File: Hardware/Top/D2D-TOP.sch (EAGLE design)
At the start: 54 parts, among them SW1 SWITCH.MOM, SW2 SWITCH.MOM, U2 NRF52832_MODULE_MDBT42, U4 PCF8523, U6 PHOTOTRANSISTOR

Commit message: current top and bottom board
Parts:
- added SW5: SWITCH.MOM, LinnesLab-Switches:SWITCH.MOM
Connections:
- removed net VBATT: U4.VBAT
- net GND: now also SW5.3, SW5.4, USB2.SHIELD
- net SW1: now also SW5.1
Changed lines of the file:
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@@
 <part name="SW2" library="LinnesLab-Switches" deviceset="SWITCH.MOM" device=""/>
 <part name="GND2" library="LinnesLab-Symbols" deviceset="GND" device=""/>
+<part name="SW5" library="LinnesLab-Switches" deviceset="SWITCH.MOM" device=""/>
+<part name="GND5" library="LinnesLab-Symbols" deviceset="GND" device=""/>
 </parts>
 <sheets>
@@
 <attribute name="VALUE" x="320.04" y="25.146" size="1.778" layer="96" align="top-center"/>
 </instance>
+<instance part="SW5" gate="G$1" x="347.98" y="33.02" smashed="yes">
+<attribute name="NAME" x="347.98" y="37.846" size="1.778" layer="95" font="vector" align="bottom-center"/>
+<attribute name="VALUE" x="347.98" y="30.226" size="1.778" layer="96" font="vector" align="top-center"/>
+</instance>
+<instance part="GND5" gate="G$1" x="355.6" y="25.4" smashed="yes">
+<attribute name="VALUE" x="355.6" y="25.146" size="1.778" layer="96" align="top-center"/>
+</instance>
 </instances>
 <busses>
@@
 <pinref part="GND40" gate="G$1" pin="GND"/>
 <wire x1="40.64" y1="-68.58" x2="40.64" y2="-76.2" width="0.1524" layer="91"/>
+<pinref part="USB2" gate="G$1" pin="SHIELD"/>
+<wire x1="38.1" y1="-55.88" x2="40.64" y2="-55.88" width="0.1524" layer="91"/>
+<wire x1="40.64" y1="-55.88" x2="40.64" y2="-68.58" width="0.1524" layer="91"/>
+<junction x="40.64" y="-68.58"/>
 </segment>
 <segment>
@@
 <wire x1="317.5" y1="30.48" x2="320.04" y2="30.48" width="0.1524" layer="91" style="longdash"/>
 <junction x="320.04" y="30.48"/>
+</segment>
+<segment>
+<pinref part="SW5" gate="G$1" pin="3"/>
+<pinref part="GND5" gate="G$1" pin="GND"/>
+<wire x1="353.06" y1="33.02" x2="355.6" y2="33.02" width="0.1524" layer="91" style="longdash"/>
+<wire x1="355.6" y1="33.02" x2="355.6" y2="30.48" width="0.1524" layer="91" style="longdash"/>
+<pinref part="SW5" gate="G$1" pin="4"/>
+<wire x1="355.6" y1="30.48" x2="355.6" y2="27.94" width="0.1524" layer="91" style="longdash"/>
+<wire x1="353.06" y1="30.48" x2="355.6" y2="30.48" width="0.1524" layer="91" style="longdash"/>
+<junction x="355.6" y="30.48"/>
 </segment>
 </net>
@@
 </segment>
 </net>
-<net name="VBATT" class="0">
-<segment>
-<wire x1="284.48" y1="-17.78" x2="281.94" y2="-17.78" width="0.1524" layer="91"/>
-<label x="281.94" y="-17.78" size="1.27" layer="95" rot="R180" xref="yes"/>
-<pinref part="U4" gate="G$1" pin="VBAT"/>
-</segment>
-</net>
 <net name="OUTPUT" class="0">
 <segment>
@@
 <label x="304.8" y="33.02" size="1.27" layer="95" ratio="15" rot="R180" xref="yes"/>
 </segment>
-</net>
+<segment>
+<pinref part="SW5" gate="G$1" pin="1"/>
+<wire x1="342.9" y1="33.02" x2="340.36" y2="33.02" width="0.1524" layer="91"/>
+<label x="340.36" y="33.02" size="1.27" layer="95" ratio="15" rot="R180" xref="yes"/>
+</segment>
+</net>

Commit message: unfinished 002
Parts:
- removed SW5: SWITCH.MOM, LinnesLab-Switches:SWITCH.MOM
- added C23: 100n, LinnesLab-Passives:CAPACITOR0603
- added C24, C25: 47p, LinnesLab-Passives:CAPACITOR0603
- added J1: (no value), LinnesLab-Connectors:CONN_07
- added JP2: (no value), LinnesLab-Switches:JUMPER-SMT_2_NO_SILK
- added LED5: RED, LinnesLab-LED:LED0603
- added LED6: YELLOW, LinnesLab-LED:LED0603
- added R1, R2: 0, LinnesLab-Passives:RESISTOR0603
- added R18, R19: 27, LinnesLab-Passives:RESISTOR0603
- added R20, R21: 1k, LinnesLab-Passives:RESISTOR0603
- added U5: FT231XS, LinnesLab-DigitalIC:FT231XS
- R9: value 10k -> (none)
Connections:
- removed net BATT: R13.1, R14.2
- removed net CHRG.STAT: CHRG2.STAT, R12.1
- removed net RXD: U2.P0.08
- removed net TXD: U2.P0.06
- new net A4/BATT: R13.1, R14.2, U2.P0.28/AIN4
- new net CTS: JP2.2, U5.!CTS
- new net D27/CHRGSTATUS: CHRG2.STAT, R12.1, U2.P0.27
- new net FT3V3: U5.3V3OUT
- new net N$23: R18.2, U5.USBDM
- new net N$24: R19.2, U5.USBDP
- new net N$25: LED5.C, R20.2
- new net N$26: LED6.C, R21.2
- new net RXD.FT: R2.1, U5.RXD
- new net RXD.NRF: R1.2, U2.P0.08
- new net RXLED: R20.1, U5.CBUS1
- new net TXD.FT: R1.1, U5.TXD
- new net TXD.NRF: R2.2, U2.P0.06
- new net TXLED: R21.1, U5.CBUS2
- net 3.3V: now also C23.2, LED5.A, LED6.A, U5.!RESET, U5.VCCIO
- net DTR: now also U5.!DTR
- net GND: now also C23.1, C24.2, C25.1, JP2.1, U5.GND@16, U5.GND@6; no longer SW5.3, SW5.4
- net SCL: now also R9.1; no longer R8.1
- net SDA: now also R8.1; no longer R9.1
- net SW1: no longer SW5.1
- net USB+: now also C24.1, R19.1
- net USB-: now also C25.2, R18.1
- net V_USB: now also U5.VCC
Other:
- note added: "I don't remember if CTS needs to be grounded or left floating so here's a jumper to ground so it can be configued either way dynamically."
- note added: "TXD goes to RX on the other device RXD goes to TX on the other device"
- moved on the sheet: R8, R9

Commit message: updated to 002
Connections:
- removed net CD1: SD2.CARD_DETECT
- removed net CS.OLED: U3./CS
- removed net DC.OLED: U3.DC/I2C_SA0
- removed net RESET.OLED: U3./RES
- removed net SD.CS: SD2.CS
- removed net SW1: SW1.1, SW2.1
- new net A6/TIA: J1.5, U2.P0.30/AIN6
- new net A7/PPG: J1.7, U2.P0.31/AIN7
- new net D11/SW1: SW1.1, U2.P0.11
- new net D15/SW2: SW2.1, U2.P0.15
- new net D16/CS.OLED: U2.P0.16, U3./CS
- new net D29/LED.CTRL: J1.6, U2.P0.29/AIN5
- new net D3/RESET.OLED: U2.P0.03/AIN1, U3./RES
- new net D4/DC.OLED: U2.P0.04/AIN2, U3.DC/I2C_SA0
- new net D5/CD1: SD2.CARD_DETECT, U2.P0.05/AIN3
- new net D7/SD.CS: SD2.CS, U2.P0.07
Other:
- note added: "FTDI Serial to USB Converter"
- moved on the sheet: C23, C24, C25, J1, JP2, LED5, LED6, R1, R18, R19, R2, R20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

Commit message: checkpoint 3
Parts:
- J1: device LinnesLab-Connectors:CONN_07 -> LinnesLab-Connectors:CONN_07-1.27MM
- renumbered CHRG2 to CHRG
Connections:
- net 3.3V: now also J1.4
- net A6/TIA: now also J1.6; no longer J1.5
- net D29/LED.CTRL: now also J1.5; no longer J1.6
- net GND: now also J1.3
- net SCL: now also J1.2
- net SDA: now also J1.1
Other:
- note added: "Connection to top board"
- moved on the sheet: J1
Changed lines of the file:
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@@
 <part name="GND22" library="LinnesLab-Symbols" deviceset="GND" device=""/>
 <part name="SD2" library="LinnesLab-Connectors" deviceset="MICROSD" device="" package3d_urn="urn:adsk.eagle:package:17873109/2"/>
-<part name="CHRG2" library="LinnesLab-Power" deviceset="MCP73831" device=""/>
+<part name="CHRG" library="LinnesLab-Power" deviceset="MCP73831" device=""/>
 <part name="LDO2" library="LinnesLab-Power" deviceset="MIC5504" device=""/>
 <part name="D4" library="LinnesLab-DiscreteSemi" deviceset="SCHOTTKY" device="-USC" package3d_urn="urn:adsk.eagle:package:15664784/2"/>
@@
 <part name="SUPPLY1" library="LinnesLab-Symbols" deviceset="3.3V" device=""/>
 <part name="SUPPLY6" library="LinnesLab-Symbols" deviceset="3.3V" device=""/>
-<part name="J1" library="LinnesLab-Connectors" deviceset="CONN_07" device=""/>
+<part name="J1" library="LinnesLab-Connectors" deviceset="CONN_07" device="-1.27MM"/>
+<part name="SUPPLY8" library="LinnesLab-Symbols" deviceset="3.3V" device=""/>
+<part name="GND5" library="LinnesLab-Symbols" deviceset="GND" device=""/>
 </parts>
 <sheets>
@@
 <wire x1="-40.64" y1="208.28" x2="172.72" y2="208.28" width="1.27" layer="97" style="longdash"/>
 <wire x1="172.72" y1="208.28" x2="172.72" y2="198.12" width="1.27" layer="97" style="longdash"/>
+<text x="7.62" y="223.52" size="1.27" layer="96">Connection to
+top board</text>
 </plain>
 <instances>
@@
 <attribute name="VALUE" x="210.82" y="-3.81" size="1.778" layer="96"/>
 </instance>
-<instance part="CHRG2" gate="G$1" x="96.52" y="-60.96" smashed="yes">
+<instance part="CHRG" gate="G$1" x="96.52" y="-60.96" smashed="yes">
 <attribute name="NAME" x="88.9" y="-55.372" size="1.778" layer="95"/>
 <attribute name="VALUE" x="88.9" y="-68.58" size="1.778" layer="96"/>
@@
 <attribute name="VALUE" x="-12.7" y="172.974" size="1.778" layer="96" align="bottom-center"/>
 </instance>
-<instance part="J1" gate="G$1" x="-10.16" y="241.3" smashed="yes">
-<attribute name="VALUE" x="-15.24" y="231.394" size="1.778" layer="96" font="vector"/>
-<attribute name="NAME" x="-15.24" y="254.508" size="1.778" layer="95" font="vector"/>
+<instance part="J1" gate="G$1" x="12.7" y="241.3" smashed="yes">
+<attribute name="VALUE" x="7.62" y="231.394" size="1.778" layer="96" font="vector"/>
+<attribute name="NAME" x="7.62" y="254.508" size="1.778" layer="95" font="vector"/>
+</instance>
+<instance part="SUPPLY8" gate="G$1" x="20.32" y="254" smashed="yes">
+<attribute name="VALUE" x="20.32" y="256.794" size="1.778" layer="96" align="bottom-center"/>
+</instance>
+<instance part="GND5" gate="G$1" x="20.32" y="231.14" smashed="yes">
+<attribute name="VALUE" x="20.32" y="230.886" size="1.778" layer="96" align="top-center"/>
 </instance>
 </instances>
@@
 </segment>
 <segment>
-<pinref part="CHRG2" gate="G$1" pin="VSS"/>
+<pinref part="CHRG" gate="G$1" pin="VSS"/>
 <wire x1="106.68" y1="-63.5" x2="109.22" y2="-63.5" width="0.1524" layer="91"/>
 <pinref part="GND43" gate="G$1" pin="GND"/>
@@
 <pinref part="GND50" gate="G$1" pin="GND"/>
 <wire x1="243.84" y1="228.6" x2="243.84" y2="226.06" width="0.1524" layer="91"/>
+</segment>
+<segment>
+<pinref part="J1" gate="G$1" pin="3"/>
+<wire x1="17.78" y1="241.3" x2="20.32" y2="241.3" width="0.1524" layer="91"/>
+<pinref part="GND5" gate="G$1" pin="GND"/>
+<wire x1="20.32" y1="233.68" x2="20.32" y2="241.3" width="0.1524" layer="91"/>
 </segment>
 </net>
@@
 <pinref part="SUPPLY6" gate="G$1" pin="3.3V"/>
 </segment>
+<segment>
+<pinref part="J1" gate="G$1" pin="4"/>
+<wire x1="17.78" y1="243.84" x2="20.32" y2="243.84" width="0.1524" layer="91"/>
+<pinref part="SUPPLY8" gate="G$1" pin="3.3V"/>
+<wire x1="20.32" y1="254" x2="20.32" y2="243.84" width="0.1524" layer="91"/>
+</segment>
 </net>
 <net name="SDA" class="0">
@@
 <label x="-25.4" y="154.94" size="1.27" layer="95" rot="R270" xref="yes"/>
 </segment>
+<segment>
+<pinref part="J1" gate="G$1" pin="1"/>
+<wire x1="17.78" y1="236.22" x2="22.86" y2="236.22" width="0.1524" layer="91"/>
+<label x="22.86" y="236.22" size="1.27" layer="95" xref="yes"/>
+</segment>
 </net>
 <net name="SCL" class="0">
@@
 <wire x1="-12.7" y1="157.48" x2="-12.7" y2="154.94" width="0.1524" layer="91"/>
 <label x="-12.7" y="154.94" size="1.27" layer="95" rot="R270" xref="yes"/>
+</segment>
+<segment>
+<pinref part="J1" gate="G$1" pin="2"/>
+<wire x1="17.78" y1="238.76" x2="22.86" y2="238.76" width="0.1524" layer="91"/>
+<label x="22.86" y="238.76" size="1.27" layer="95" xref="yes"/>
 </segment>
 </net>
@@
 <net name="N$17" class="0">
 <segment>
-<pinref part="CHRG2" gate="G$1" pin="PROG"/>
+<pinref part="CHRG" gate="G$1" pin="PROG"/>
 <wire x1="106.68" y1="-60.96" x2="116.84" y2="-60.96" width="0.1524" layer="91"/>
 <pinref part="R11" gate="G$1" pin="2"/>
@@
 </segment>
 <segment>
-<pinref part="CHRG2" gate="G$1" pin="VBAT"/>
+<pinref part="CHRG" gate="G$1" pin="VBAT"/>
 <wire x1="106.68" y1="-58.42" x2="124.46" y2="-58.42" width="0.1524" layer="91"/>
 <pinref part="C20" gate="G$1" pin="1"/>
@@
 <wire x1="63.5" y1="-58.42" x2="63.5" y2="-25.4" width="0.1524" layer="91"/>
 <junction x="63.5" y="-25.4"/>
-<pinref part="CHRG2" gate="G$1" pin="VIN"/>
+<pinref part="CHRG" gate="G$1" pin="VIN"/>
 <wire x1="86.36" y1="-58.42" x2="78.74" y2="-58.42" width="0.1524" layer="91"/>
 <junction x="63.5" y="-58.42"/>
@@
 <wire x1="78.74" y1="-76.2" x2="83.82" y2="-76.2" width="0.1524" layer="91"/>
 <wire x1="83.82" y1="-76.2" x2="83.82" y2="-63.5" width="0.1524" layer="91"/>
-<pinref part="CHRG2" gate="G$1" pin="STAT"/>
+<pinref part="CHRG" gate="G$1" pin="STAT"/>
 <wire x1="83.82" y1="-63.5" x2="86.36" y2="-63.5" width="0.1524" layer="91"/>
 <label x="83.82" y="-76.2" size="1.27" layer="95" xref="yes"/>
@@
 </segment>
 <segment>
-<pinref part="J1" gate="G$1" pin="6"/>
-<wire x1="-5.08" y1="248.92" x2="-2.54" y2="248.92" width="0.1524" layer="91" style="longdash"/>
-<label x="-2.54" y="248.92" size="1.27" layer="95" xref="yes"/>
+<pinref part="J1" gate="G$1" pin="5"/>
+<wire x1="17.78" y1="246.38" x2="22.86" y2="246.38" width="0.1524" layer="91"/>
+<label x="22.86" y="246.38" size="1.27" layer="95" xref="yes"/>
 </segment>
 </net>
@@
 </segment>
 <segment>
-<pinref part="J1" gate="G$1" pin="5"/>
-<wire x1="-5.08" y1="246.38" x2="-2.54" y2="246.38" width="0.1524" layer="91" style="longdash"/>
-<label x="-2.54" y="246.38" size="1.27" layer="95" xref="yes"/>
+<pinref part="J1" gate="G$1" pin="6"/>
+<wire x1="17.78" y1="248.92" x2="22.86" y2="248.92" width="0.1524" layer="91"/>
+<label x="22.86" y="248.92" size="1.27" layer="95" xref="yes"/>
 </segment>
 </net>
@@
 <segment>
 <pinref part="J1" gate="G$1" pin="7"/>
-<wire x1="-5.08" y1="251.46" x2="-2.54" y2="251.46" width="0.1524" layer="91" style="longdash"/>
-<label x="-2.54" y="251.46" size="1.27" layer="95" xref="yes"/>
-</segment>
-</net>
+<wire x1="17.78" y1="251.46" x2="22.86" y2="251.46" width="0.1524" layer="91"/>
+<label x="22.86" y="251.46" size="1.27" layer="95" xref="yes"/>
+</segment>
+</net>

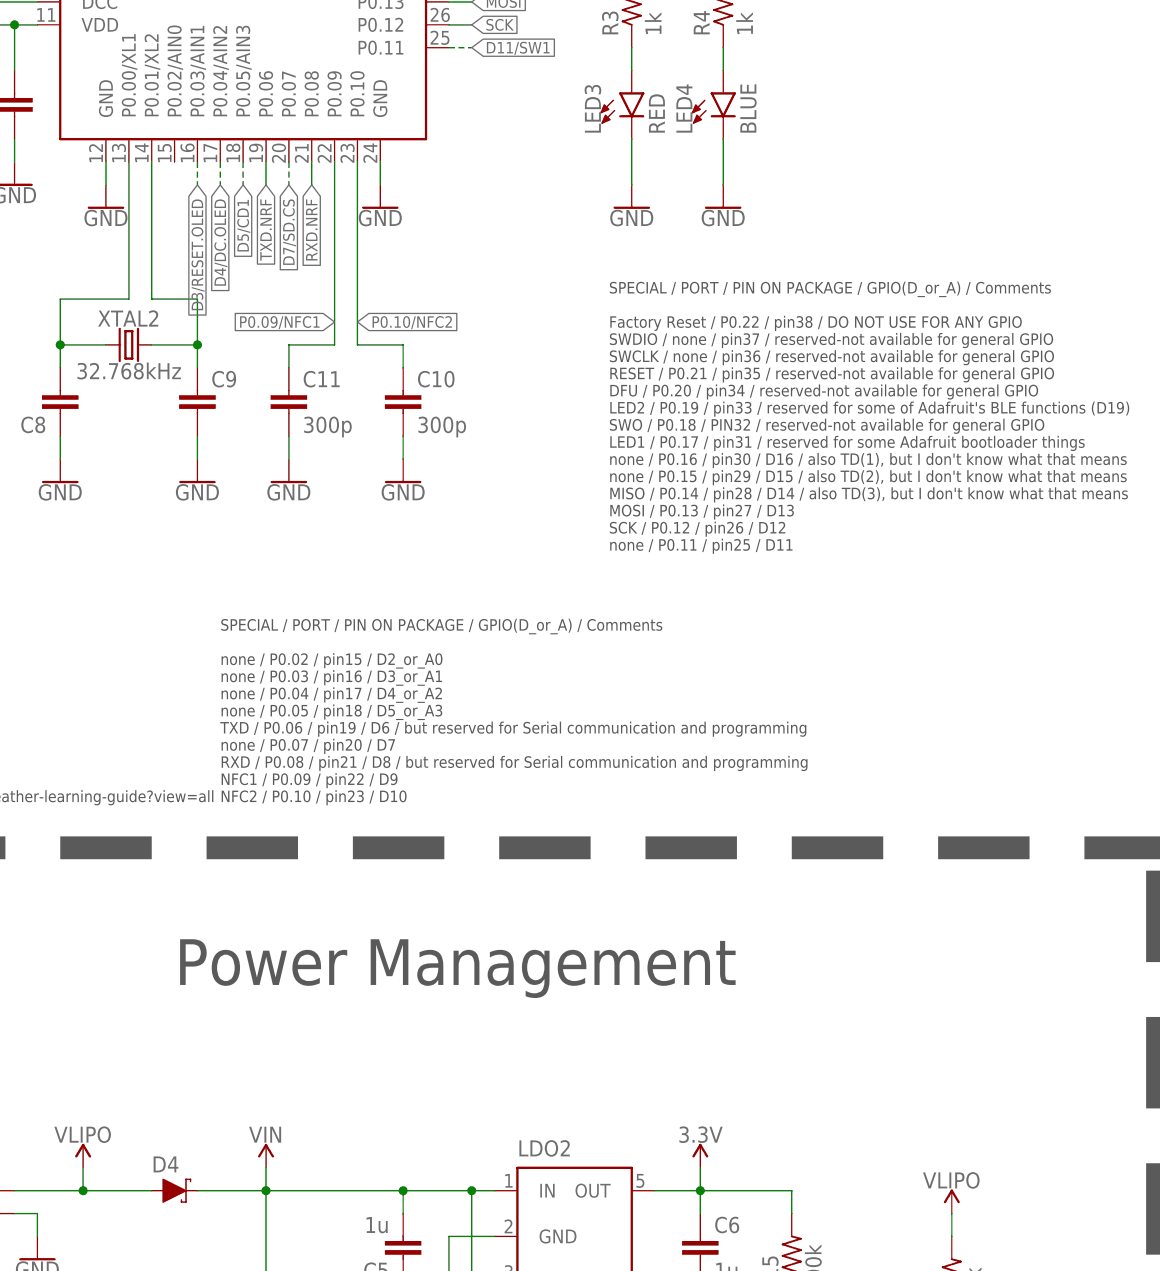
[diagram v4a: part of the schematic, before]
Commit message: added starting code
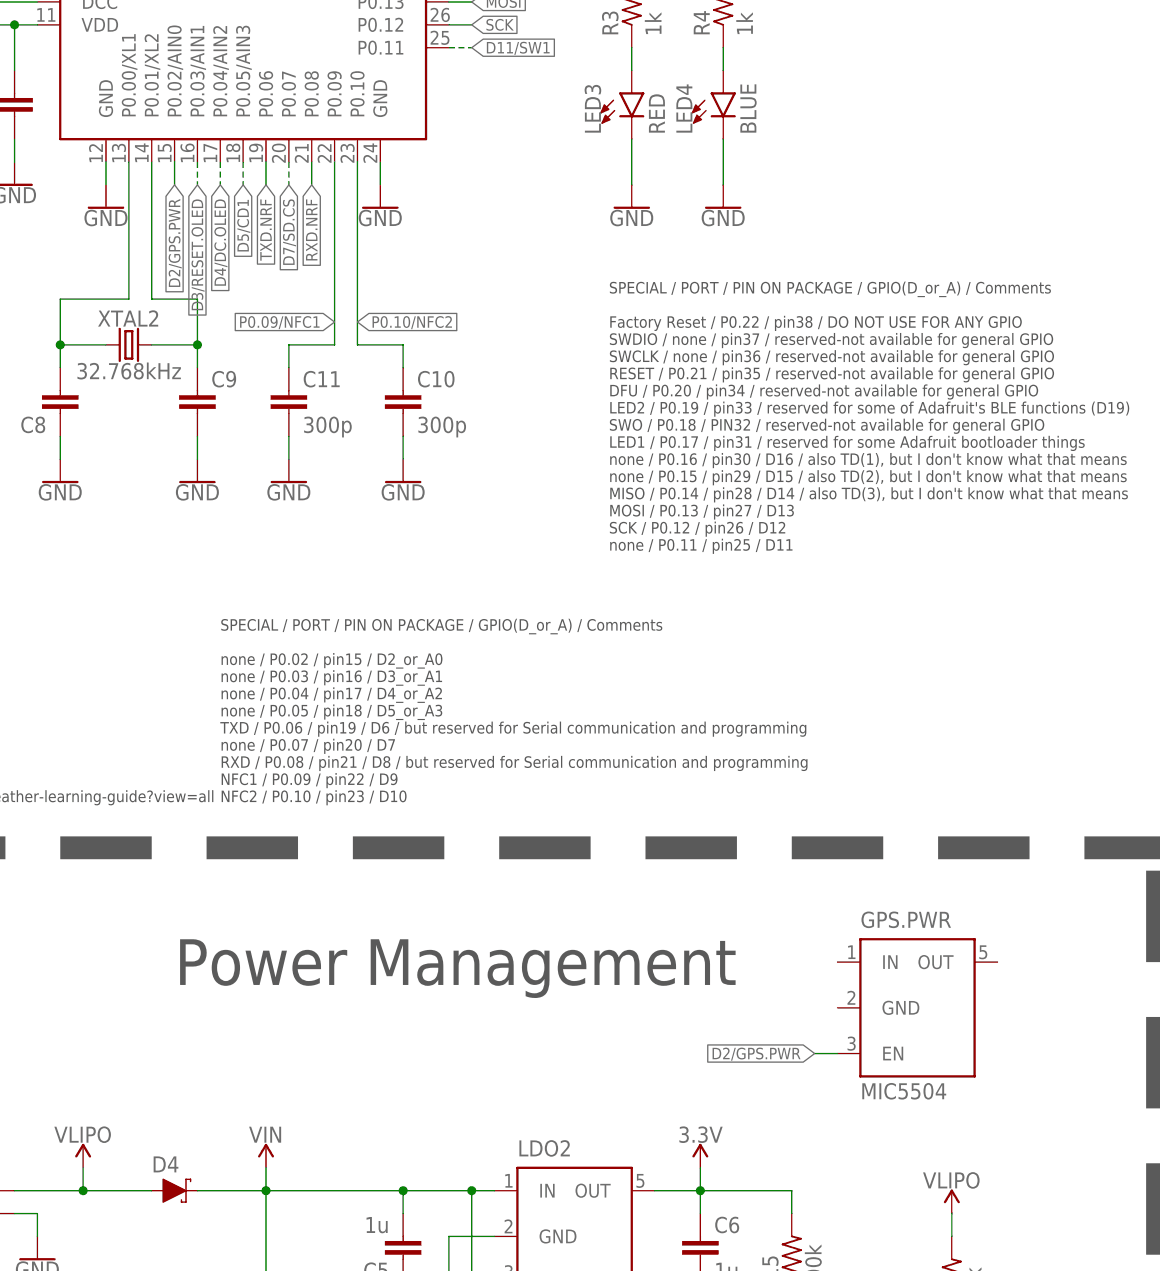
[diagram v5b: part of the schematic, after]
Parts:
- added GPS.PWR: MIC5504, LinnesLab-Power:MIC5504
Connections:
- new net D2/GPS.PWR: GPS.PWR.EN, U2.P0.02/AIN0
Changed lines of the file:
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@@
 <part name="SUPPLY8" library="LinnesLab-Symbols" deviceset="3.3V" device=""/>
 <part name="GND5" library="LinnesLab-Symbols" deviceset="GND" device=""/>
+<part name="GPS.PWR" library="LinnesLab-Power" deviceset="MIC5504" device=""/>
 </parts>
 <sheets>
@@
 <attribute name="VALUE" x="20.32" y="230.886" size="1.778" layer="96" align="top-center"/>
 </instance>
+<instance part="GPS.PWR" gate="G$1" x="137.16" y="-5.08" smashed="yes">
+<attribute name="NAME" x="129.54" y="3.81" size="1.778" layer="95"/>
+<attribute name="VALUE" x="129.54" y="-15.24" size="1.778" layer="96"/>
+</instance>
 </instances>
 <busses>
@@
 </segment>
 </net>
+<net name="D2/GPS.PWR" class="0">
+<segment>
+<pinref part="U2" gate="G$1" pin="P0.02/AIN0"/>
+<wire x1="53.34" y1="88.9" x2="53.34" y2="86.36" width="0.1524" layer="91"/>
+<label x="53.34" y="86.36" size="1.27" layer="95" rot="R270" xref="yes"/>
+</segment>
+<segment>
+<pinref part="GPS.PWR" gate="G$1" pin="EN"/>
+<wire x1="127" y1="-10.16" x2="124.46" y2="-10.16" width="0.1524" layer="91"/>
+<label x="124.46" y="-10.16" size="1.27" layer="95" rot="R180" xref="yes"/>
+</segment>
+</net>
